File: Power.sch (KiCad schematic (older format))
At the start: 0 parts

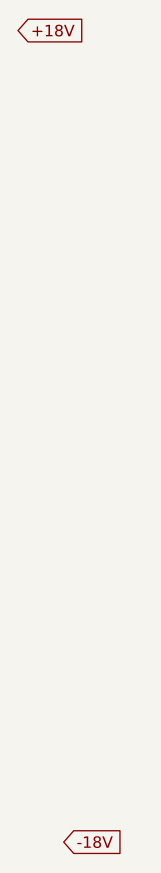
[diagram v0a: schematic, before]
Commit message: Rename power flags for consistency
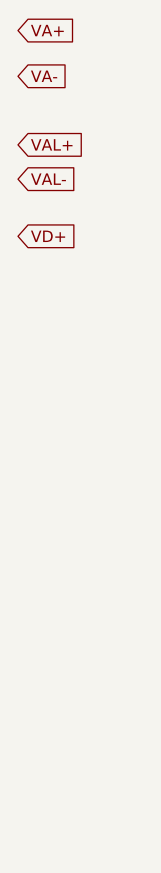
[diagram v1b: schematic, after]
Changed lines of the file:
@@
 $EndDescr
 Text GLabel 9250 1800 2    50   Input ~ 0
-+18V
-Text GLabel 9450 5350 2    50   Input ~ 0
--18V
+VA+
+Text GLabel 9250 2000 2    50   Input ~ 0
+VA-
+Text GLabel 9250 2300 2    50   Input ~ 0
+VAL+
+Text GLabel 9250 2450 2    50   Input ~ 0
+VAL-
+Text GLabel 9250 2700 2    50   Input ~ 0
+VD+
 $EndSCHEMATC

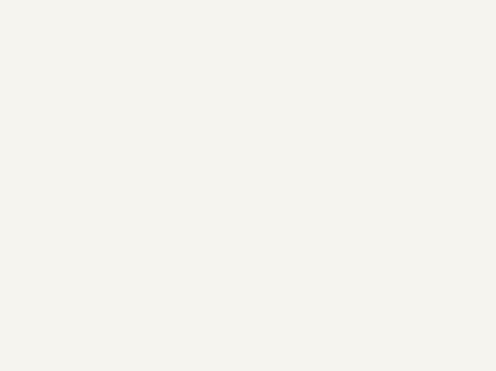
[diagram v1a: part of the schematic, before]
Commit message: Add net tie between AGND and DGND
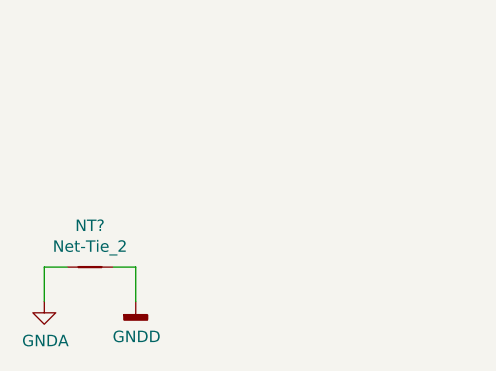
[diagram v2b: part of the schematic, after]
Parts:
- added NT?: Net-Tie_2, symbol Device:Net-Tie_2
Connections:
- new net GNDA: NT?.1
- new net GNDD: NT?.2
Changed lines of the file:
@@
 Text GLabel 9250 2700 2    50   Input ~ 0
 VD+
+$Comp
+L Device:Net-Tie_2 NT?
+U 1 1 5E71464A
+P 1500 7050
+F 0 "NT?" H 1500 7231 50  0000 C CNN
+F 1 "Net-Tie_2" H 1500 7140 50  0000 C CNN
+F 2 "" H 1500 7050 50  0001 C CNN
+F 3 "~" H 1500 7050 50  0001 C CNN
+	1    1500 7050
+	1    0    0    -1
+$EndComp
+$Comp
+L power:GNDA #PWR?
+U 1 1 5E7152E3
+P 1300 7200
+F 0 "#PWR?" H 1300 6950 50  0001 C CNN
+F 1 "GNDA" H 1305 7027 50  0000 C CNN
+F 2 "" H 1300 7200 50  0001 C CNN
+F 3 "" H 1300 7200 50  0001 C CNN
+	1    1300 7200
+	1    0    0    -1
+$EndComp
+$Comp
+L power:GNDD #PWR?
+U 1 1 5E715913
+P 1700 7200
+F 0 "#PWR?" H 1700 6950 50  0001 C CNN
+F 1 "GNDD" H 1704 7045 50  0000 C CNN
+F 2 "" H 1700 7200 50  0001 C CNN
+F 3 "" H 1700 7200 50  0001 C CNN
+	1    1700 7200
+	1    0    0    -1
+$EndComp
+Wire Wire Line
+	1600 7050 1700 7050
+Wire Wire Line
+	1700 7050 1700 7200
+Wire Wire Line
+	1400 7050 1300 7050
+Wire Wire Line
+	1300 7050 1300 7200
 $EndSCHEMATC
